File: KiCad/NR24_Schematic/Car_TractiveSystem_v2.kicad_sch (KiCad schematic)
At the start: 15 parts, among them J1 M_con, J2 F_con, K2 Key Switch Relay, M1 Zero_7R_Motor, SW3 100V E-stop (Right), SW4 100V E-stop (Left), SW7 TI power switch, SW8 GLVMS, U1 Sevcon_Gen4_Size6, U2 Throttle, U7 Brake (AiM Pressure Sensor)

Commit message: .
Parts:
- 3A: value Fuse -> 3A Fuse
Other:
- sheet Dash ports: added Battery Lights; removed IMD Light
- moved on the sheet: J1, J2, K2, LA6, M1, SW3, SW4, SW8

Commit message: Now it is pretty :)
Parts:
- removed LA6: TSAL, symbol Device:Lamp
- added LA5: TSAL, symbol Device:Lamp
- U7: value Brake (AiM Pressure Sensor) -> Brake Pressure Sensor (Aim)
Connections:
- net Earth: now also LA5.1 (-)
- new net TSAL_Logic/TSAL Voltage: LA5.2 (+)
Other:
- added sheet TSAL_Logic (TSAL_Logic.kicad_sch)
- sheet Battery_High: file AMS.kicad_sch -> Battery_High.kicad_sch
- sheet Battery_High ports: added Dash_Error_AMS +, Dash_Error_AMS -, Dash_Error_IMD +, Dash_Error_IMD -; removed Dash_Error +, Dash_Error -
- sheet Dash ports: added none; removed GND
- sheet Ti Board ports: added Break Sensor Input, To Dash; removed none
- note added: "Back of Car"
- note added: "Behind Dash"
- note added: "Chassis GND = LV GND"
- note added: "In Front of Driver"
- note added: "Left Side of Driver"
- note added: "Mounted to Top of Frame"
- note added: "Near Sevcon"
- note added: "On top, back of Car"
- note added: "Right Side of Driver"
- note added: "To Charger (Not Defined)"
- note removed: "ABC or ACB"
- note removed: "Mounted to Frame"
- moved on the sheet: BTaux1, SW3, SW4, SW7, SW8

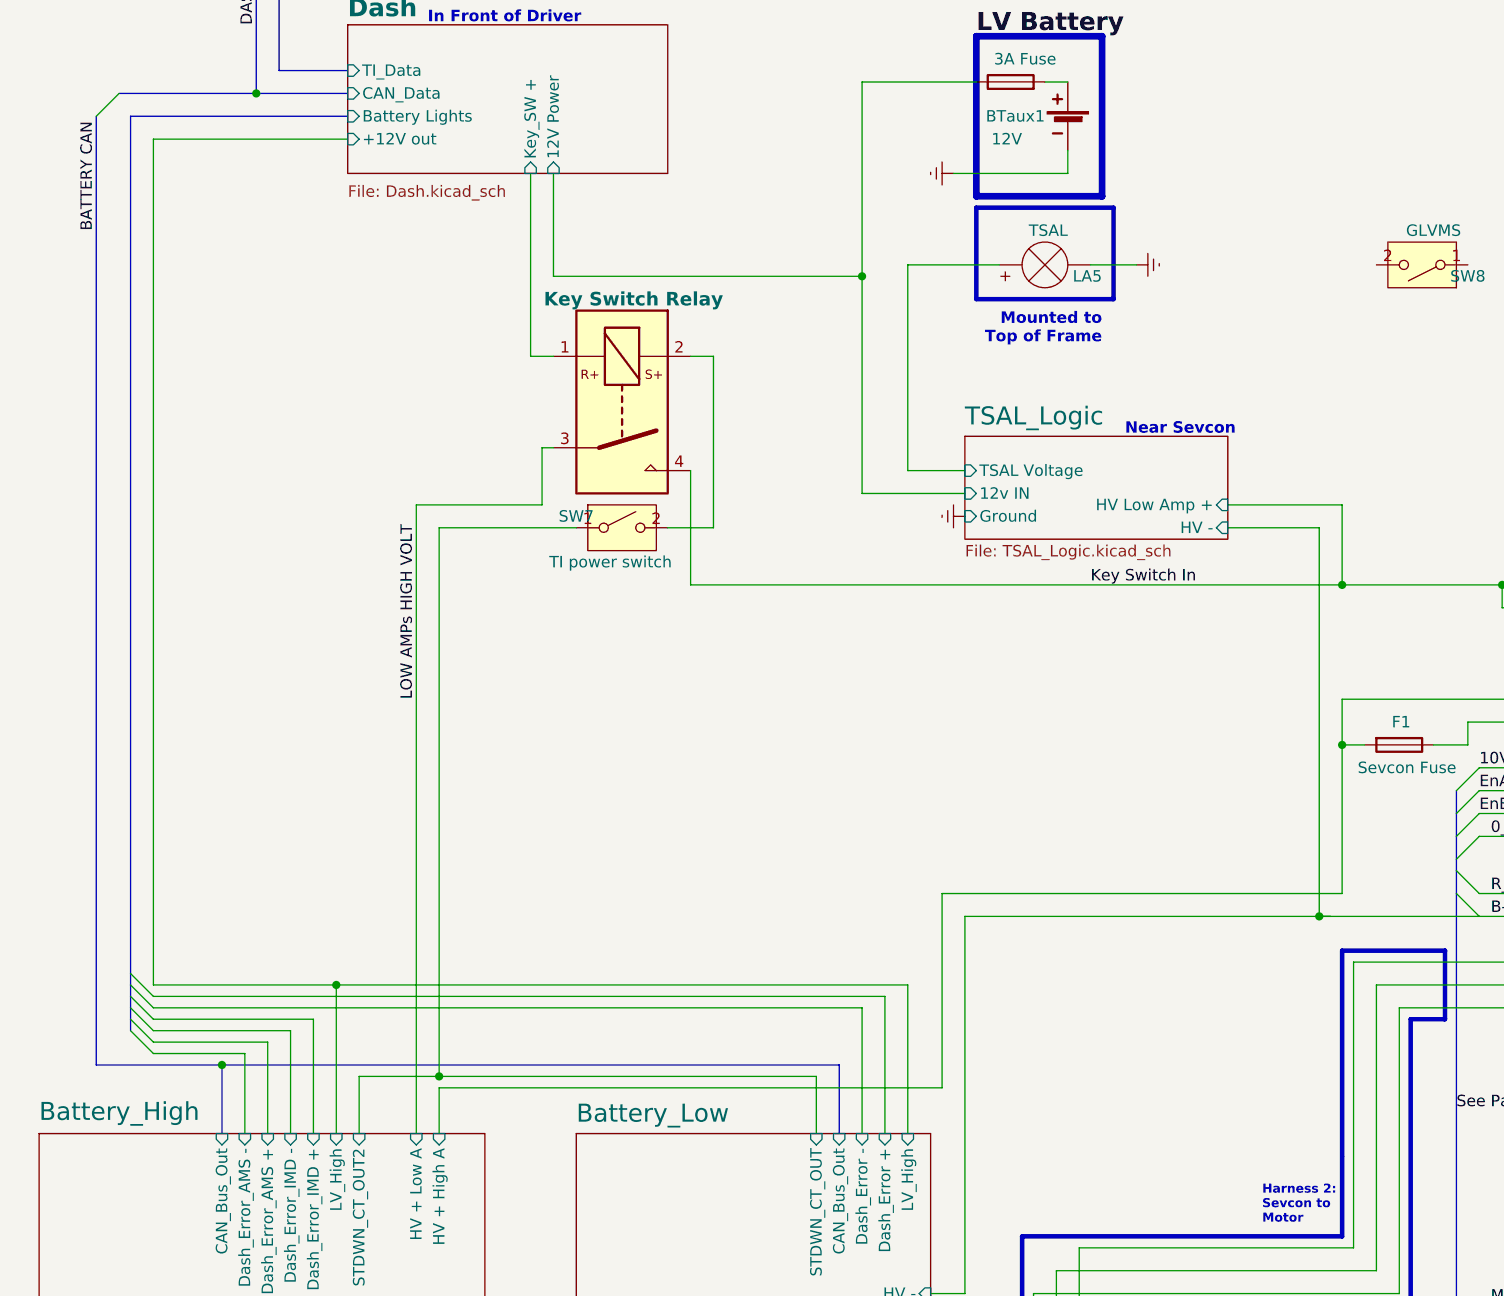
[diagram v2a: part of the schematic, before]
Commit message: Added VDM
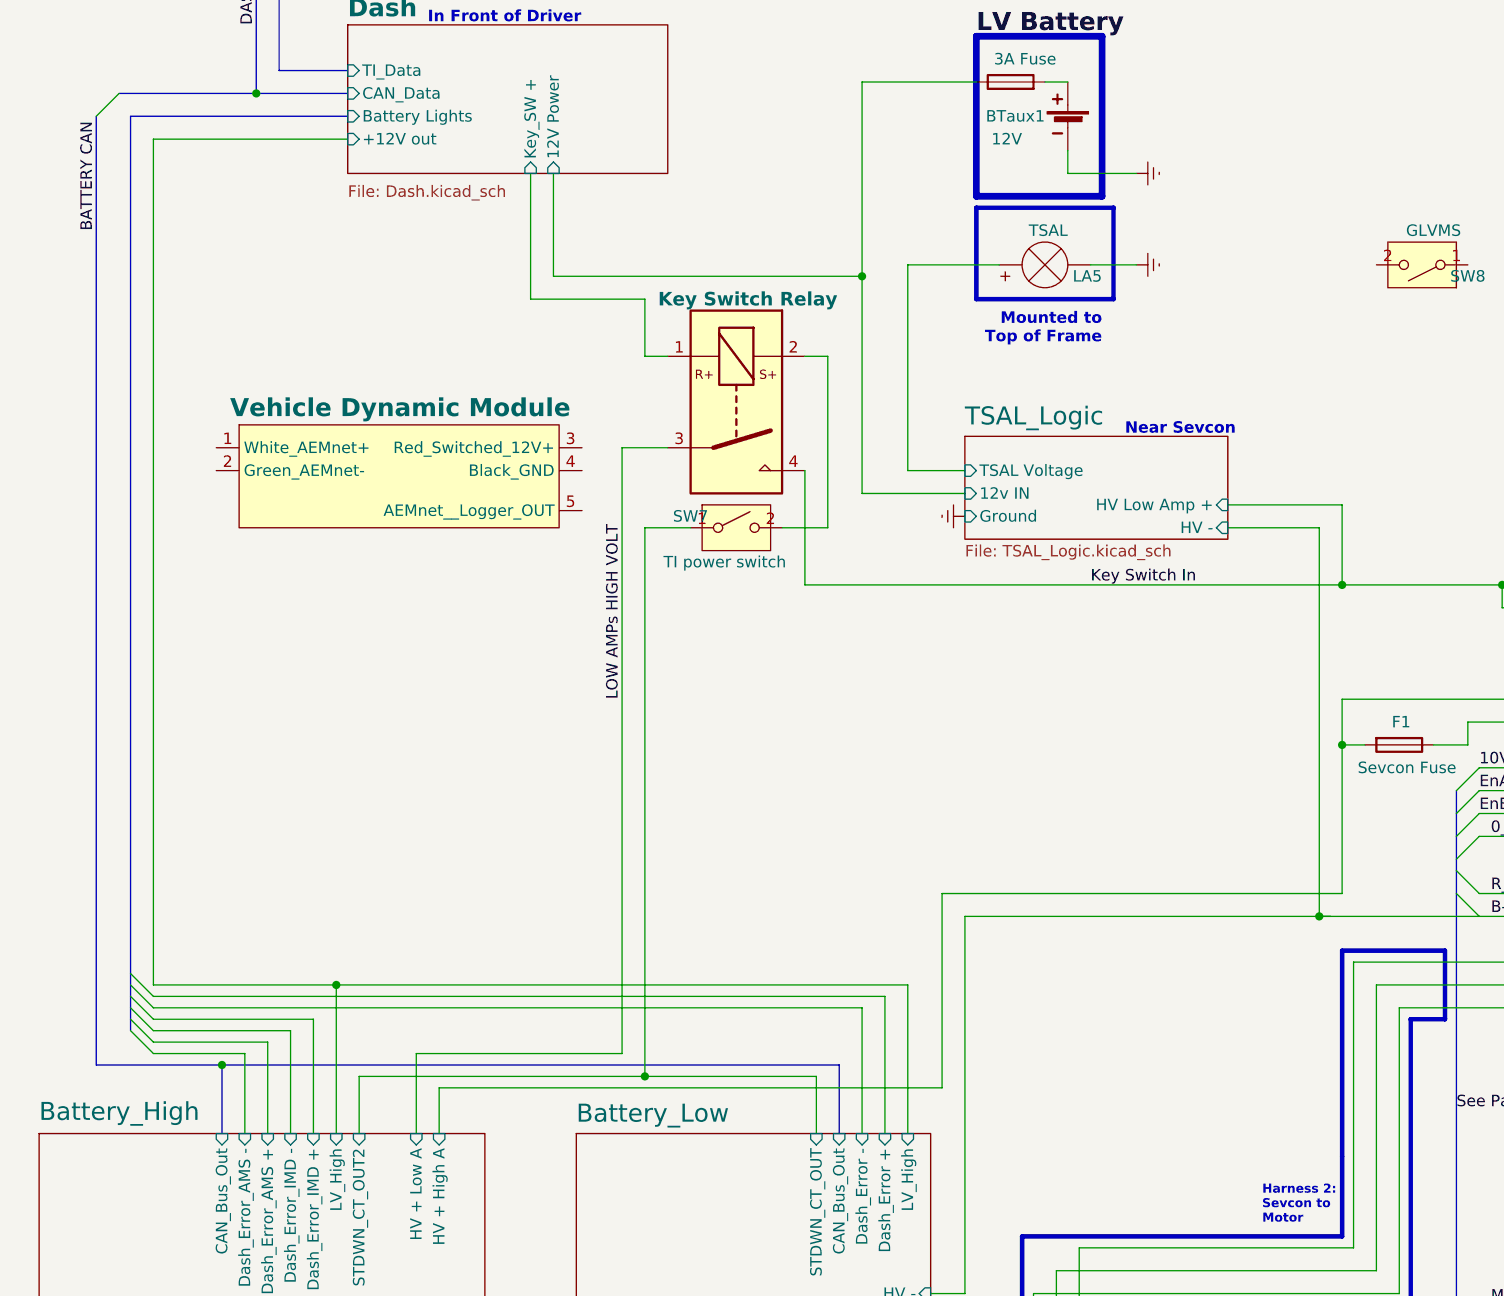
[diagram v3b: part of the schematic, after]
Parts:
- added U4: Vehicle Dynamic Module, symbol CamachosSymbols:Sevcon_Gen4_Size6
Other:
- moved on the sheet: SW7
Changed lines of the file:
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@@
   (junction (at 54.61 220.98) (diameter 0) (color 0 0 0 0)
   )
+  (junction (at 88.9 231.14) (diameter 0) (color 0 0 0 0)
+  )
   (junction (at 241.3 204.47) (diameter 0) (color 0 0 0 0)
   )
@@
   )
   (junction (at 166.37 176.53) (diameter 0) (color 0 0 0 0)
-  )
-  (junction (at 66.04 231.14) (diameter 0) (color 0 0 0 0)
   )
   (junction (at 184.15 176.53) (diameter 0) (color 0 0 0 0)
@@
     (stroke (width 0) (type default))
   )
-  (wire (pts (xy 76.2 130.81) (xy 76.2 151.13))
+  (wire (pts (xy 88.9 144.78) (xy 88.9 151.13))
     (stroke (width 0) (type default))
   )
@@
     (stroke (width 0.5) (type default) (color 255 153 0 1))
   )
+  (wire (pts (xy 88.9 144.78) (xy 76.2 144.78))
+    (stroke (width 0) (type default))
+  )
   (wire (pts (xy 181.61 213.36) (xy 186.69 213.36))
     (stroke (width 0.75) (type default))
   )
-  (wire (pts (xy 77.47 161.29) (xy 78.74 161.29))
-    (stroke (width 0.5) (type default))
+  (wire (pts (xy 86.36 161.29) (xy 91.44 161.29))
+    (stroke (width 0.5) (type default))
+  )
+  (wire (pts (xy 76.2 144.78) (xy 76.2 130.81))
+    (stroke (width 0) (type default))
   )
   (bus (pts (xy 48.26 119.38) (xy 55.88 119.38))
     (stroke (width 0) (type default))
   )
-  (wire (pts (xy 77.47 167.64) (xy 77.47 161.29))
+  (wire (pts (xy 63.5 228.6) (xy 63.5 237.49))
     (stroke (width 0.5) (type default))
   )
@@
   (wire (pts (xy 189.23 273.05) (xy 176.53 273.05))
     (stroke (width 0) (type default))
-  )
-  (wire (pts (xy 63.5 167.64) (xy 77.47 167.64))
-    (stroke (width 0.5) (type default))
   )
   (bus (pts (xy 31.75 124.46) (xy 31.75 219.71))
@@
     (stroke (width 0) (type default))
   )
-  (wire (pts (xy 66.04 170.18) (xy 81.28 170.18))
+  (wire (pts (xy 88.9 170.18) (xy 93.98 170.18))
     (stroke (width 0) (type default))
   )
@@
     (stroke (width 0) (type default))
   )
+  (wire (pts (xy 86.36 228.6) (xy 63.5 228.6))
+    (stroke (width 0.5) (type default))
+  )
   (wire (pts (xy 34.29 223.52) (xy 113.03 223.52))
     (stroke (width 0) (type default))
@@
     (stroke (width 0) (type default))
   )
-  (wire (pts (xy 76.2 151.13) (xy 78.74 151.13))
+  (wire (pts (xy 88.9 151.13) (xy 91.44 151.13))
     (stroke (width 0) (type default))
   )
@@
     (stroke (width 0) (type default))
   )
-  (wire (pts (xy 66.04 231.14) (xy 107.95 231.14))
-    (stroke (width 0) (type default))
-  )
   (bus (pts (xy 179.07 256.54) (xy 210.82 256.54))
     (stroke (width 0) (type default))
@@
     (stroke (width 0) (type default))
   )
-  (wire (pts (xy 93.98 176.53) (xy 166.37 176.53))
+  (wire (pts (xy 106.68 176.53) (xy 166.37 176.53))
     (stroke (width 0.5) (type default))
   )
@@
     (stroke (width 0.5) (type default))
   )
-  (wire (pts (xy 63.5 167.64) (xy 63.5 237.49))
+  (wire (pts (xy 86.36 161.29) (xy 86.36 228.6))
     (stroke (width 0.5) (type default))
   )
@@
     (stroke (width 0) (type default))
   )
-  (wire (pts (xy 57.15 231.14) (xy 66.04 231.14))
+  (wire (pts (xy 57.15 231.14) (xy 88.9 231.14))
     (stroke (width 0) (type default))
   )
@@
     (stroke (width 0) (type default))
   )
-  (wire (pts (xy 93.98 176.53) (xy 93.98 163.83))
+  (wire (pts (xy 106.68 176.53) (xy 106.68 163.83))
     (stroke (width 0.5) (type default))
   )
@@
     (stroke (width 0.75) (type solid))
   )
-  (wire (pts (xy 123.19 130.81) (xy 135.89 130.81))
+  (wire (pts (xy 143.51 130.81) (xy 135.89 130.81))
     (stroke (width 0) (type default))
   )
@@
     (stroke (width 0) (type default))
   )
-  (wire (pts (xy 91.44 170.18) (xy 96.52 170.18))
+  (wire (pts (xy 104.14 170.18) (xy 109.22 170.18))
     (stroke (width 0) (type default))
   )
@@
     (stroke (width 0) (type default))
   )
-  (wire (pts (xy 66.04 170.18) (xy 66.04 231.14))
+  (wire (pts (xy 88.9 231.14) (xy 107.95 231.14))
+    (stroke (width 0) (type default))
+  )
+  (wire (pts (xy 88.9 170.18) (xy 88.9 231.14))
     (stroke (width 0) (type default))
   )
@@
     (stroke (width 0.75) (type default))
   )
-  (wire (pts (xy 96.52 151.13) (xy 96.52 170.18))
+  (wire (pts (xy 109.22 151.13) (xy 109.22 170.18))
     (stroke (width 0) (type default))
   )
@@
     (stroke (width 0) (type default))
   )
-  (wire (pts (xy 93.98 151.13) (xy 96.52 151.13))
+  (wire (pts (xy 106.68 151.13) (xy 109.22 151.13))
     (stroke (width 0) (type default))
   )
@@
     (effects (font (size 1.27 1.27)) (justify right bottom))
   )
-  (label "LOW AMPs HIGH VOLT" (at 63.5 189.23 90) (fields_autoplaced)
+  (label "LOW AMPs HIGH VOLT" (at 86.36 189.23 90) (fields_autoplaced)
     (effects (font (size 1.27 1.27)) (justify left bottom))
   )
@@
     )
   )
+  (symbol (lib_name "Sevcon_Gen4_Size6_1") (lib_id "CamachosSymbols:Sevcon_Gen4_Size6") (at 60.96 165.1 0) (unit 1)
+    (in_bom yes) (on_board yes) (dnp no)
+    (property "Reference" "U4" (at 60.96 171.45 0)
+      (effects (font (size 1.27 1.27)) hide)
+    )
+    (property "Value" "Vehicle Dynamic Module" (at 80.645 156.845 0)
+      (effects (font (size 2 2) bold) (justify right))
+    )
+    (property "Footprint" "" (at 42.545 196.85 0)
+      (effects (font (size 1.27 1.27) italic) hide)
+    )
+    (property "Datasheet" "" (at 42.545 196.85 0)
+      (effects (font (size 1.27 1.27)) hide)
+    )
+    (pin "1")
+    (pin "2")
+    (pin "3")
+    (pin "4")
+    (pin "5")
+    (instances
+      (project "Car_TractiveSystem_v2"
+        (path "/588b5c14-1813-4e1d-9dbe-940839ecebe3"
+          (reference "U4") (unit 1)
+        )
+      )
+    )
+  )
   (symbol (lib_id "Device:Battery_Cell") (at 135.89 125.73 0) (mirror y) (unit 1)
     (in_bom yes) (on_board yes) (dnp no)
@@
     )
   )
-  (symbol (lib_id "CamachosSymbols:SW_SPST") (at 86.36 170.18 0) (unit 1)
-    (in_bom yes) (on_board yes) (dnp no)
-    (property "Reference" "SW7" (at 81.28 168.91 0)
+  (symbol (lib_id "CamachosSymbols:SW_SPST") (at 99.06 170.18 0) (unit 1)
+    (in_bom yes) (on_board yes) (dnp no)
+    (property "Reference" "SW7" (at 93.98 168.91 0)
       (effects (font (size 1.27 1.27)))
     )
-    (property "Value" "TI power switch" (at 85.09 173.99 0)
+    (property "Value" "TI power switch" (at 97.79 173.99 0)
       (effects (font (size 1.27 1.27)))
     )
-    (property "Footprint" "" (at 86.36 170.18 0)
-      (effects (font (size 1.27 1.27)) hide)
-    )
-    (property "Datasheet" "~" (at 86.36 170.18 0)
+    (property "Footprint" "" (at 99.06 170.18 0)
+      (effects (font (size 1.27 1.27)) hide)
+    )
+    (property "Datasheet" "~" (at 99.06 170.18 0)
       (effects (font (size 1.27 1.27)) hide)
     )
@@
     )
   )
-  (symbol (lib_id "Relay:ADW11") (at 85.09 157.48 0) (unit 1)
-    (in_bom yes) (on_board yes) (dnp no)
-    (property "Reference" "K2" (at 77.47 153.67 0)
-      (effects (font (size 1.27 1.27)) hide)
-    )
-    (property "Value" "Key Switch Relay" (at 87.63 144.78 0)
+  (symbol (lib_id "Relay:ADW11") (at 97.79 157.48 0) (unit 1)
+    (in_bom yes) (on_board yes) (dnp no)
+    (property "Reference" "K2" (at 90.17 153.67 0)
+      (effects (font (size 1.27 1.27)) hide)
+    )
+    (property "Value" "Key Switch Relay" (at 100.33 144.78 0)
       (effects (font (size 1.5 1.5) bold))
     )
-    (property "Footprint" "Relay_THT:Relay_1P1T_NO_10x24x18.8mm_Panasonic_ADW11xxxxW_THT" (at 86.36 123.825 0)
-      (effects (font (size 1.27 1.27)) hide)
-    )
-    (property "Datasheet" "https://www.panasonic-electric-works.com/pew/es/downloads/ds_dw_hl_en.pdf" (at 105.41 154.94 90)
+    (property "Footprint" "Relay_THT:Relay_1P1T_NO_10x24x18.8mm_Panasonic_ADW11xxxxW_THT" (at 99.06 123.825 0)
+      (effects (font (size 1.27 1.27)) hide)
+    )
+    (property "Datasheet" "https://www.panasonic-electric-works.com/pew/es/downloads/ds_dw_hl_en.pdf" (at 118.11 154.94 90)
       (effects (font (size 1.27 1.27)) hide)
     )
@@
     )
   )
-  (symbol (lib_id "power:Earth") (at 123.19 130.81 270) (unit 1)
+  (symbol (lib_id "power:Earth") (at 143.51 130.81 90) (mirror x) (unit 1)
     (in_bom yes) (on_board yes) (dnp no) (fields_autoplaced)
-    (property "Reference" "#PWR01" (at 116.84 130.81 0)
-      (effects (font (size 1.27 1.27)) hide)
-    )
-    (property "Value" "Earth" (at 119.38 130.81 0)
-      (effects (font (size 1.27 1.27)) hide)
-    )
-    (property "Footprint" "" (at 123.19 130.81 0)
-      (effects (font (size 1.27 1.27)) hide)
-    )
-    (property "Datasheet" "~" (at 123.19 130.81 0)
-      (effects (font (size 1.27 1.27)) hide)
-    )
+    (property "Reference" "#PWR01" (at 149.86 130.81 0)
+      (effects (font (size 1.27 1.27)) hide)
+    )
+    (property "Value" "Earth" (at 147.32 130.81 0)
+      (effects (font (size 1.27 1.27)) hide)
+    )
+    (property "Footprint" "" (at 143.51 130.81 0)
+      (effects (font (size 1.27 1.27)) hide)
+    )
+    (property "Datasheet" "~" (at 143.51 130.81 0)
+      (effects (font (size 1.27 1.27)) hide)
+    )
